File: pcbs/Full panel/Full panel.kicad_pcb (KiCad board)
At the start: 2 copper layers, 1 part, among them Q1 Si2319CDS

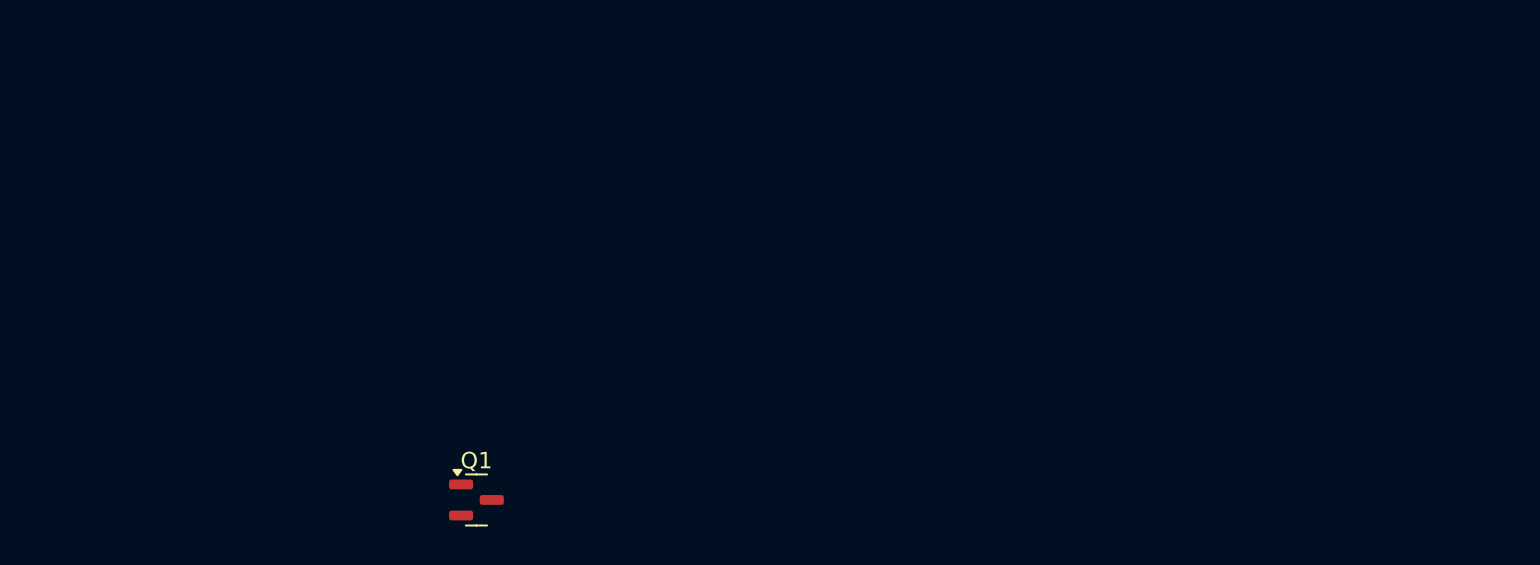
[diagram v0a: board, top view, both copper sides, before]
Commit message: Full Pannel With lt3519 for low voltage application
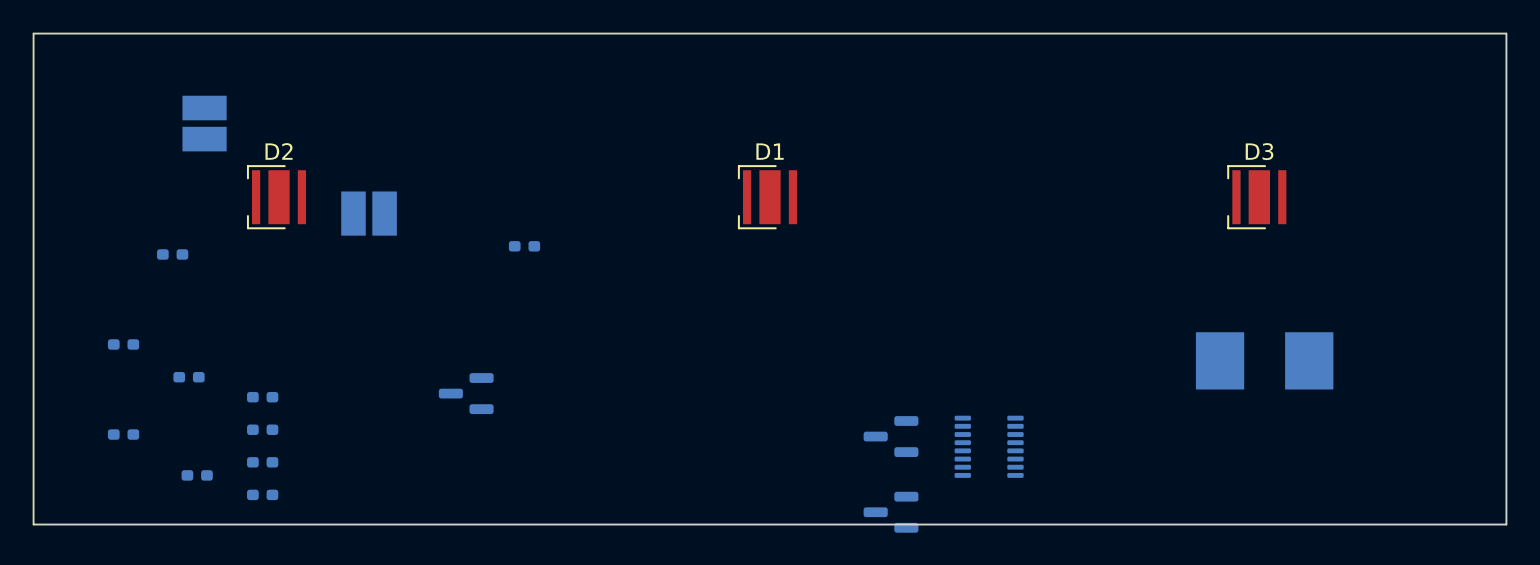
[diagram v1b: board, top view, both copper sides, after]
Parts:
- added C1: 4.7uF, digikey-footprints:SMD-2_3.2x2.5mm, B.Cu at (90.5, 50.5)
- added C2: 10uF, digikey-footprints:SMD-2_3.2x2.5mm, B.Cu at (100.5, 56.0)
- added D1: LED, LED_SMD:LED_Cree-XP, F.Cu at (125.0, 55.0)
- added D2: LED, LED_SMD:LED_Cree-XP, F.Cu at (95.0, 55.0)
- added D3: LED, LED_SMD:LED_Cree-XP, F.Cu at (154.9, 55.0)
- added L1: 47uH, Inductor_SMD:L_Bourns_SRP7028A_7.3x6.6mm, B.Cu at (155.2, 65.0)
- added Q1: PNP, Package_TO_SOT_SMD:SOT-23, B.Cu at (132.4, 69.6)
- added Q2: NPN, Package_TO_SOT_SMD:SOT-23, B.Cu at (132.4, 74.2)
- added R1: 100k, Resistor_SMD:R_0402_1005Metric_Pad0.72x0.64mm_HandSolder, B.Cu at (88.5, 58.5)
- added R10: 1k, Resistor_SMD:R_0402_1005Metric_Pad0.72x0.64mm_HandSolder, B.Cu at (94.0, 73.2)
- added R2: 1M, Resistor_SMD:R_0402_1005Metric_Pad0.72x0.64mm_HandSolder, B.Cu at (85.5, 64.0)
- added R3: 191k, Resistor_SMD:R_0402_1005Metric_Pad0.72x0.64mm_HandSolder, B.Cu at (85.5, 69.5)
- added R4: 0.5, Resistor_SMD:R_0402_1005Metric_Pad0.72x0.64mm_HandSolder, B.Cu at (89.5, 66.0)
- added R5: 130k, Resistor_SMD:R_0402_1005Metric_Pad0.72x0.64mm_HandSolder, B.Cu at (90.0, 72.0)
- added R6: 10k, Resistor_SMD:R_0402_1005Metric_Pad0.72x0.64mm_HandSolder, B.Cu at (110.0, 58.0)
- added R7: 14.7k, Resistor_SMD:R_0402_1005Metric_Pad0.72x0.64mm_HandSolder, B.Cu at (94.0, 67.2)
- added R8: 1M, Resistor_SMD:R_0402_1005Metric_Pad0.72x0.64mm_HandSolder, B.Cu at (94.0, 69.2)
- added R9: 1.5k, Resistor_SMD:R_0402_1005Metric_Pad0.72x0.64mm_HandSolder, B.Cu at (94.0, 71.2)
- added U1: LT 3519, ganzfeld_fp:ST3519, B.Cu at (138.4, 70.5)
- M1: renamed from Q1; moved to B.Cu
- moved M1 6.53 mm to (106.4, 67.0), turned to 180 degrees
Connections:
- M1 pad 1: unconnected-(Q1-G-Pad1) -> Net-(M1-G)
- M1 pad 2: LED+ -> Net-(M1-S)
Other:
- board outline added: 90 x 30 mm
